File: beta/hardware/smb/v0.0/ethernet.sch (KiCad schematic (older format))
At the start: 20 parts, among them J201 HR911105_RJ45, U201 ENC28J60, X201 25MHz

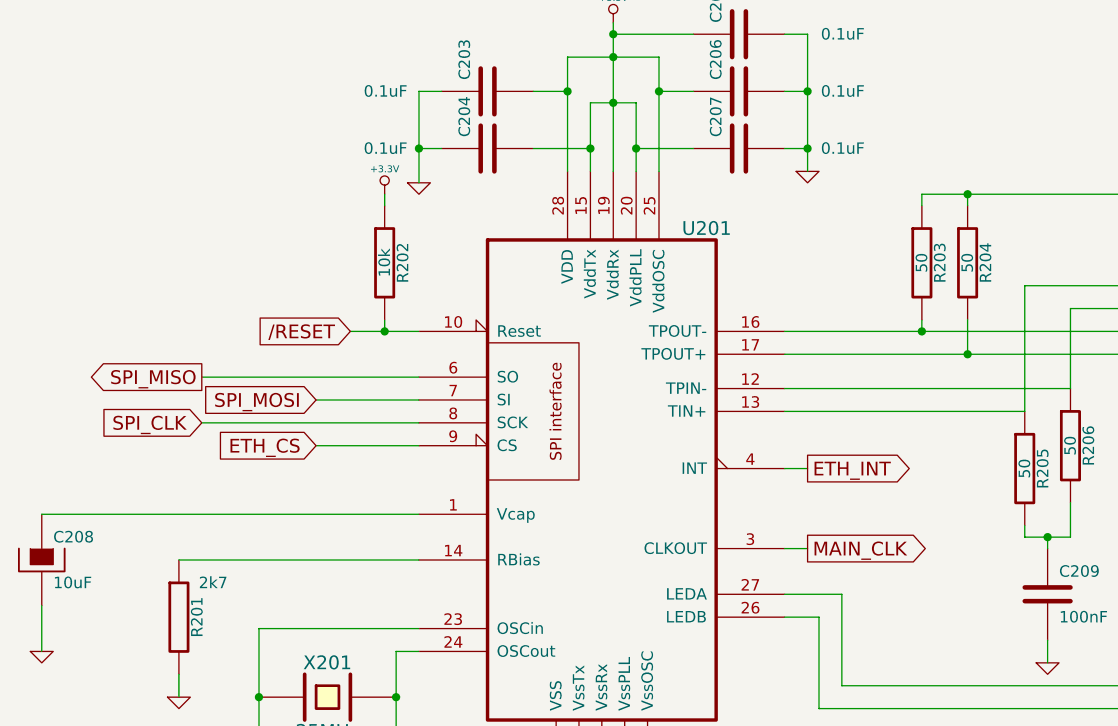
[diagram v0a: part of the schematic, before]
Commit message: SPI, clock, I2C, Misc schematic upgrade
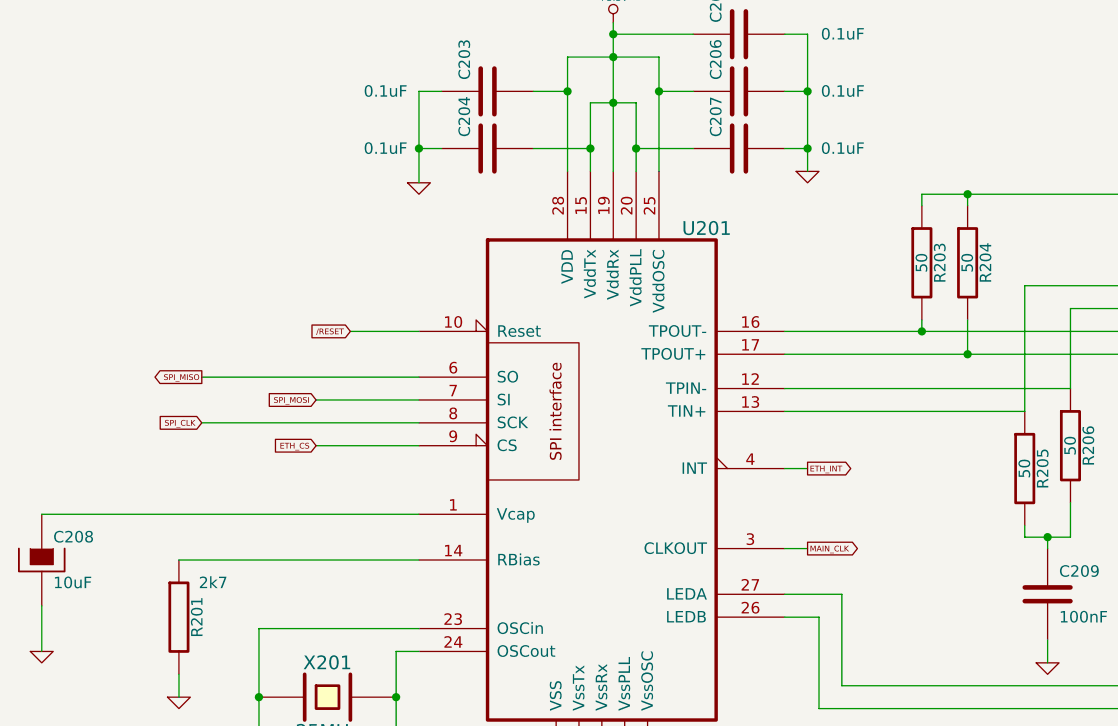
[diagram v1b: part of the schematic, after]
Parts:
- removed R202: 10k, symbol R
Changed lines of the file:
@@
-EESchema Schematic File Version 2  date 01/05/2012 18:36:30
+EESchema Schematic File Version 2  date 02/05/2012 01:38:42
 LIBS:power
 LIBS:device
@@
 LIBS:valves
 LIBS:hr911105_rj45
+LIBS:Small_connectors
 LIBS:SMB-cache
 EELAYER 25  0
@@
 	7900 3050 6650 3050
 Wire Wire Line
-	4900 2800 4900 2750
-Wire Wire Line
 	6750 3400 6650 3400
 Wire Wire Line
@@
 	6650 3750 6750 3750
 Wire Wire Line
-	4900 2200 4900 2250
-Wire Wire Line
 	4750 2800 5050 2800
-Connection ~ 4900 2800
 Wire Wire Line
 	6650 3150 7700 3150
@@
 $EndComp
 $Comp
-L +3.3V #PWR211
+L +3.3V #PWR05
 U 1 1 4FA00F89
 P 8550 1500
-F 0 "#PWR211" H 8550 1460 30  0001 C CNN
+F 0 "#PWR05" H 8550 1460 30  0001 C CNN
 F 1 "+3.3V" H 8550 1610 30  0000 C CNN
 	1    8550 1500
@@
 $EndComp
 $Comp
-L GND #PWR212
+L GND #PWR06
 U 1 1 4FA00F53
 P 8550 3700
-F 0 "#PWR212" H 8550 3700 30  0001 C CNN
+F 0 "#PWR06" H 8550 3700 30  0001 C CNN
 F 1 "GND" H 8550 3630 30  0001 C CNN
 	1    8550 3700
@@
 $EndComp
 $Comp
-L GND #PWR213
+L GND #PWR07
 U 1 1 4FA00C7B
 P 9450 3900
-F 0 "#PWR213" H 9450 3900 30  0001 C CNN
+F 0 "#PWR07" H 9450 3900 30  0001 C CNN
 F 1 "GND" H 9450 3830 30  0001 C CNN
 	1    9450 3900
@@
 $EndComp
 $Comp
-L GND #PWR214
+L GND #PWR08
 U 1 1 4FA00C63
 P 10300 4350
-F 0 "#PWR214" H 10300 4350 30  0001 C CNN
+F 0 "#PWR08" H 10300 4350 30  0001 C CNN
 F 1 "GND" H 10300 4280 30  0001 C CNN
 	1    10300 4350
@@
 $EndComp
 $Comp
-L GND #PWR210
+L GND #PWR09
 U 1 1 4F9FF676
 P 7800 4250
-F 0 "#PWR210" H 7800 4250 30  0001 C CNN
+F 0 "#PWR09" H 7800 4250 30  0001 C CNN
 F 1 "GND" H 7800 4180 30  0001 C CNN
 	1    7800 4250
@@
 	1    0    0    -1
 $EndComp
-Text GLabel 4750 2800 0    60   Input ~ 0
+Text GLabel 4750 2800 0    25   Input ~ 0
 /RESET
-$Comp
-L +3.3V #PWR204
-U 1 1 4F9FF3CF
-P 4900 2200
-F 0 "#PWR204" H 4900 2160 30  0001 C CNN
-F 1 "+3.3V" H 4900 2310 30  0000 C CNN
-	1    4900 2200
-	1    0    0    -1
-$EndComp
-$Comp
-L R R202
-U 1 1 4F9FF39B
-P 4900 2500
-F 0 "R202" V 4980 2500 50  0000 C CNN
-F 1 "10k" V 4900 2500 50  0000 C CNN
-	1    4900 2500
-	1    0    0    -1
-$EndComp
-Text GLabel 6750 3400 2    60   Output ~ 0
+Text GLabel 6750 3400 2    25   Output ~ 0
 ETH_INT
-Text GLabel 6750 3750 2    60   Output ~ 0
+Text GLabel 6750 3750 2    25   Output ~ 0
 MAIN_CLK
-Text GLabel 4100 3000 0    60   Output ~ 0
+Text GLabel 4100 3000 0    25   Output ~ 0
 SPI_MISO
-Text GLabel 4600 3100 0    60   Input ~ 0
+Text GLabel 4600 3100 0    25   Input ~ 0
 SPI_MOSI
-Text GLabel 4600 3300 0    60   Input ~ 0
+Text GLabel 4600 3300 0    25   Input ~ 0
 ETH_CS
-Text GLabel 4100 3200 0    60   Input ~ 0
+Text GLabel 4100 3200 0    25   Input ~ 0
 SPI_CLK
 $Comp
-L GND #PWR201
+L GND #PWR011
 U 1 1 4F9FEE21
 P 3400 4200
-F 0 "#PWR201" H 3400 4200 30  0001 C CNN
+F 0 "#PWR011" H 3400 4200 30  0001 C CNN
 F 1 "GND" H 3400 4130 30  0001 C CNN
 	1    3400 4200
@@
 $EndComp
 $Comp
-L GND #PWR202
+L GND #PWR012
 U 1 1 4F9FEE1E
 P 4000 4400
-F 0 "#PWR202" H 4000 4400 30  0001 C CNN
+F 0 "#PWR012" H 4000 4400 30  0001 C CNN
 F 1 "GND" H 4000 4330 30  0001 C CNN
 	1    4000 4400
@@
 $EndComp
 $Comp
-L GND #PWR206
+L GND #PWR013
 U 1 1 4F9FC462
 P 5050 2150
-F 0 "#PWR206" H 5050 2150 30  0001 C CNN
+F 0 "#PWR013" H 5050 2150 30  0001 C CNN
 F 1 "GND" H 5050 2080 30  0001 C CNN
 	1    5050 2150
@@
 $EndComp
 $Comp
-L GND #PWR209
+L GND #PWR014
 U 1 1 4F9FC45C
 P 6750 2100
-F 0 "#PWR209" H 6750 2100 30  0001 C CNN
+F 0 "#PWR014" H 6750 2100 30  0001 C CNN
 F 1 "GND" H 6750 2030 30  0001 C CNN
 	1    6750 2100
@@
 $EndComp
 $Comp
-L +3.3V #PWR208
+L +3.3V #PWR015
 U 1 1 4F9FC2EE
 P 5900 1450
-F 0 "#PWR208" H 5900 1410 30  0001 C CNN
+F 0 "#PWR015" H 5900 1410 30  0001 C CNN
 F 1 "+3.3V" H 5900 1560 30  0000 C CNN
 	1    5900 1450
@@
 $EndComp
 $Comp
-L GND #PWR203
+L GND #PWR016
 U 1 1 4F9D7261
 P 4350 5050
-F 0 "#PWR203" H 4350 5050 30  0001 C CNN
+F 0 "#PWR016" H 4350 5050 30  0001 C CNN
 F 1 "GND" H 4350 4980 30  0001 C CNN
 	1    4350 5050
@@
 $EndComp
 $Comp
-L GND #PWR205
+L GND #PWR017
 U 1 1 4F9D725B
 P 4950 5050
-F 0 "#PWR205" H 4950 5050 30  0001 C CNN
+F 0 "#PWR017" H 4950 5050 30  0001 C CNN
 F 1 "GND" H 4950 4980 30  0001 C CNN
 	1    4950 5050
@@
 $EndComp
 $Comp
-L GND #PWR207
+L GND #PWR018
 U 1 1 4F9D6E29
 P 5850 4950
-F 0 "#PWR207" H 5850 4950 30  0001 C CNN
+F 0 "#PWR018" H 5850 4950 30  0001 C CNN
 F 1 "GND" H 5850 4880 30  0001 C CNN
 	1    5850 4950

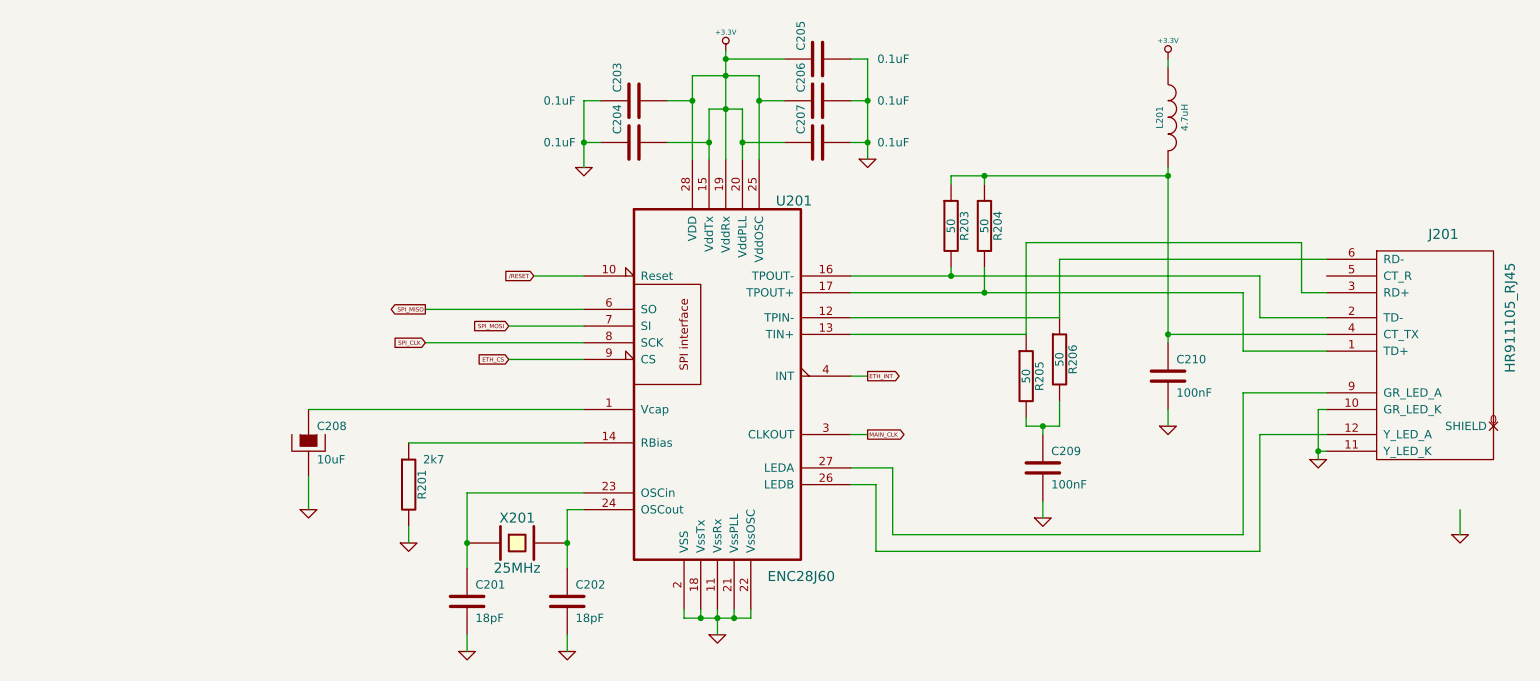
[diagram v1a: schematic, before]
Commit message: Some work on the SMD version of the SMB
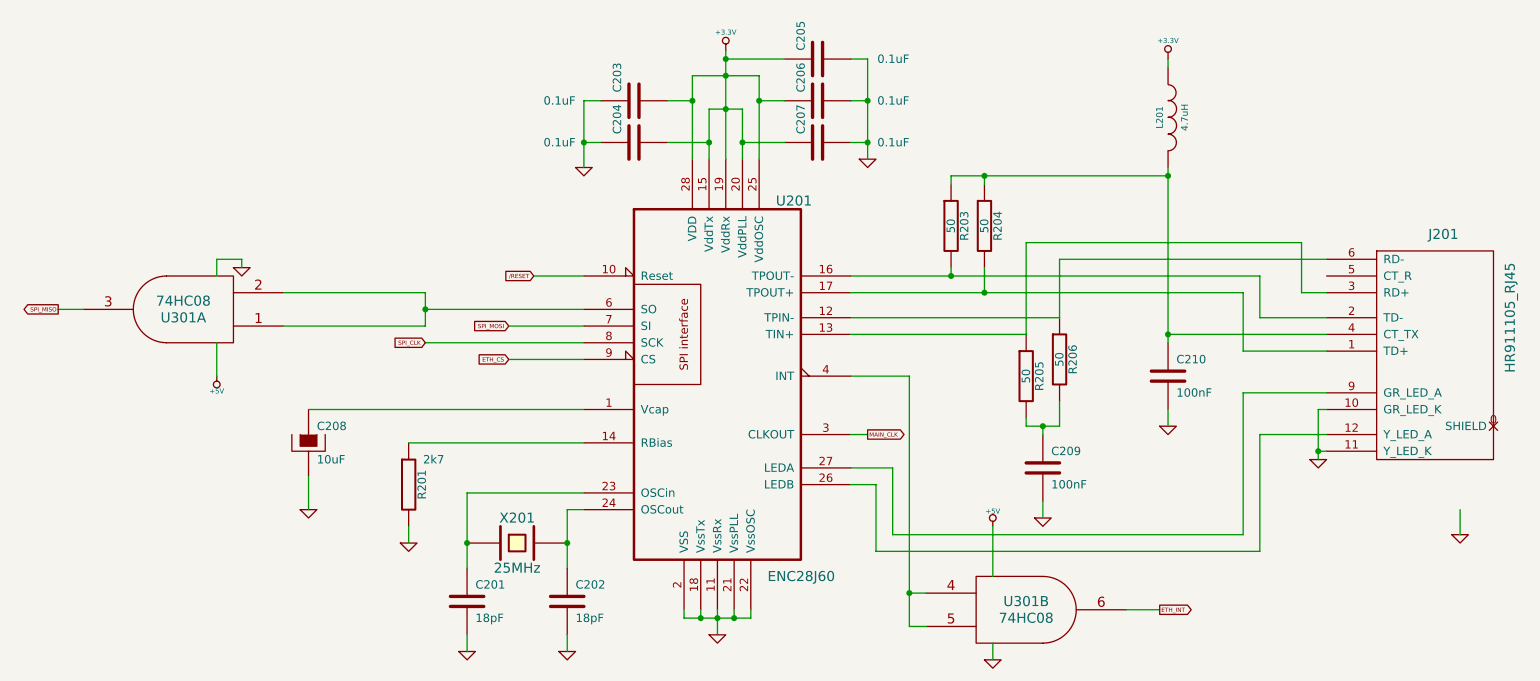
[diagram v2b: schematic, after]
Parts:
- added U301: 74HC08, symbol 74HC08
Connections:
- net ETH_INT: now also U301.6; no longer U201.4 (INT)
- net GND: now also U301.7 (GND), U301.7 (GND)
- net SPI_MISO: now also U301.3; no longer U201.6 (SO)
- new net: U201.4 (INT), U301.4, U301.5
- new net: U201.6 (SO), U301.1, U301.2
- new net +5V: U301.14 (VCC), U301.14 (VCC)
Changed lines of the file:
@@
-EESchema Schematic File Version 2  date 02/05/2012 01:38:42
+EESchema Schematic File Version 2  date 17/06/2012 23:05:58
 LIBS:power
 LIBS:device
@@
 LIBS:hr911105_rj45
 LIBS:Small_connectors
+LIBS:74hc08
+LIBS:lm1117imp-3
 LIBS:SMB-cache
 EELAYER 25  0
@@
 $Descr A4 11700 8267
 encoding utf-8
-Sheet 2 2
+Sheet 3 3
 Title ""
-Date "1 may 2012"
+Date "17 jun 2012"
 Rev ""
 Comp ""
@@
 Comment4 ""
 $EndDescr
+Wire Wire Line
+	7500 4300 7500 4600
+Wire Wire Line
+	3000 2750 3000 2700
+Wire Wire Line
+	3000 2700 2850 2700
+Wire Wire Line
+	2850 2700 2850 2800
+Wire Wire Line
+	8300 4800 8500 4800
+Wire Wire Line
+	7100 4900 7000 4900
+Wire Wire Line
+	7000 4900 7000 3400
+Wire Wire Line
+	7000 3400 6650 3400
+Connection ~ 4100 3000
+Wire Wire Line
+	3250 3100 4100 3100
+Wire Wire Line
+	4100 3100 4100 2900
 Connection ~ 8550 2200
 Wire Wire Line
@@
 	7900 3050 6650 3050
 Wire Wire Line
-	6750 3400 6650 3400
-Wire Wire Line
 	4600 3300 5050 3300
 Wire Wire Line
@@
 	7250 2200 7250 2250
 Connection ~ 7450 2200
+Wire Wire Line
+	4100 2900 3250 2900
+Wire Wire Line
+	2050 3000 1900 3000
+Wire Wire Line
+	7100 4700 7000 4700
+Connection ~ 7000 4700
+Wire Wire Line
+	2850 3200 2850 3400
+Wire Wire Line
+	7500 5000 7500 5100
+$Comp
+L +5V #PWR311
+U 1 1 4FDE1BE4
+P 7500 4300
+F 0 "#PWR311" H 7500 4390 20  0001 C CNN
+F 1 "+5V" H 7500 4390 30  0000 C CNN
+	1    7500 4300
+	1    0    0    -1
+$EndComp
+$Comp
+L GND #PWR312
+U 1 1 4FDE1B8D
+P 7500 5100
+F 0 "#PWR312" H 7500 5100 30  0001 C CNN
+F 1 "GND" H 7500 5030 30  0001 C CNN
+	1    7500 5100
+	1    0    0    -1
+$EndComp
+$Comp
+L GND #PWR302
+U 1 1 4FDE1B70
+P 3000 2750
+F 0 "#PWR302" H 3000 2750 30  0001 C CNN
+F 1 "GND" H 3000 2680 30  0001 C CNN
+	1    3000 2750
+	1    0    0    -1
+$EndComp
+$Comp
+L +5V #PWR301
+U 1 1 4FDE1B61
+P 2850 3400
+F 0 "#PWR301" H 2850 3490 20  0001 C CNN
+F 1 "+5V" H 2850 3490 30  0000 C CNN
+	1    2850 3400
+	-1   0    0    1
+$EndComp
+$Comp
+L 74HC08 U301
+U 2 1 4FDE1879
+P 7700 4800
+F 0 "U301" H 7700 4850 60  0000 C CNN
+F 1 "74HC08" H 7700 4750 60  0000 C CNN
+	2    7700 4800
+	1    0    0    -1
+$EndComp
+$Comp
+L 74HC08 U301
+U 1 1 4FDE1808
+P 2650 3000
+F 0 "U301" H 2650 3050 60  0000 C CNN
+F 1 "74HC08" H 2650 2950 60  0000 C CNN
+	1    2650 3000
+	-1   0    0    1
+$EndComp
 $Comp
 L R R204
@@
 $EndComp
 $Comp
-L +3.3V #PWR05
+L +3.3V #PWR314
 U 1 1 4FA00F89
 P 8550 1500
-F 0 "#PWR05" H 8550 1460 30  0001 C CNN
+F 0 "#PWR314" H 8550 1460 30  0001 C CNN
 F 1 "+3.3V" H 8550 1610 30  0000 C CNN
 	1    8550 1500
@@
 $EndComp
 $Comp
-L GND #PWR06
+L GND #PWR315
 U 1 1 4FA00F53
 P 8550 3700
-F 0 "#PWR06" H 8550 3700 30  0001 C CNN
+F 0 "#PWR315" H 8550 3700 30  0001 C CNN
 F 1 "GND" H 8550 3630 30  0001 C CNN
 	1    8550 3700
@@
 $EndComp
 $Comp
-L GND #PWR07
+L GND #PWR316
 U 1 1 4FA00C7B
 P 9450 3900
-F 0 "#PWR07" H 9450 3900 30  0001 C CNN
+F 0 "#PWR316" H 9450 3900 30  0001 C CNN
 F 1 "GND" H 9450 3830 30  0001 C CNN
 	1    9450 3900
@@
 $EndComp
 $Comp
-L GND #PWR08
+L GND #PWR317
 U 1 1 4FA00C63
 P 10300 4350
-F 0 "#PWR08" H 10300 4350 30  0001 C CNN
+F 0 "#PWR317" H 10300 4350 30  0001 C CNN
 F 1 "GND" H 10300 4280 30  0001 C CNN
 	1    10300 4350
@@
 $EndComp
 $Comp
-L GND #PWR09
+L GND #PWR313
 U 1 1 4F9FF676
 P 7800 4250
-F 0 "#PWR09" H 7800 4250 30  0001 C CNN
+F 0 "#PWR313" H 7800 4250 30  0001 C CNN
 F 1 "GND" H 7800 4180 30  0001 C CNN
 	1    7800 4250
@@
 Text GLabel 4750 2800 0    25   Input ~ 0
 /RESET
-Text GLabel 6750 3400 2    25   Output ~ 0
+Text GLabel 8500 4800 2    25   Output ~ 0
 ETH_INT
 Text GLabel 6750 3750 2    25   Output ~ 0
 MAIN_CLK
-Text GLabel 4100 3000 0    25   Output ~ 0
+Text GLabel 1900 3000 0    25   Output ~ 0
 SPI_MISO
 Text GLabel 4600 3100 0    25   Input ~ 0
@@
 SPI_CLK
 $Comp
-L GND #PWR011
+L GND #PWR303
 U 1 1 4F9FEE21
 P 3400 4200
-F 0 "#PWR011" H 3400 4200 30  0001 C CNN
+F 0 "#PWR303" H 3400 4200 30  0001 C CNN
 F 1 "GND" H 3400 4130 30  0001 C CNN
 	1    3400 4200
@@
 $EndComp
 $Comp
-L GND #PWR012
+L GND #PWR304
 U 1 1 4F9FEE1E
 P 4000 4400
-F 0 "#PWR012" H 4000 4400 30  0001 C CNN
+F 0 "#PWR304" H 4000 4400 30  0001 C CNN
 F 1 "GND" H 4000 4330 30  0001 C CNN
 	1    4000 4400
@@
 $EndComp
 $Comp
-L GND #PWR013
+L GND #PWR307
 U 1 1 4F9FC462
 P 5050 2150
-F 0 "#PWR013" H 5050 2150 30  0001 C CNN
+F 0 "#PWR307" H 5050 2150 30  0001 C CNN
 F 1 "GND" H 5050 2080 30  0001 C CNN
 	1    5050 2150
@@
 $EndComp
 $Comp
-L GND #PWR014
+L GND #PWR310
 U 1 1 4F9FC45C
 P 6750 2100
-F 0 "#PWR014" H 6750 2100 30  0001 C CNN
+F 0 "#PWR310" H 6750 2100 30  0001 C CNN
 F 1 "GND" H 6750 2030 30  0001 C CNN
 	1    6750 2100
@@
 $EndComp
 $Comp
-L +3.3V #PWR015
+L +3.3V #PWR309
 U 1 1 4F9FC2EE
 P 5900 1450
-F 0 "#PWR015" H 5900 1410 30  0001 C CNN
+F 0 "#PWR309" H 5900 1410 30  0001 C CNN
 F 1 "+3.3V" H 5900 1560 30  0000 C CNN
 	1    5900 1450
@@
 $EndComp
 $Comp
-L GND #PWR016
+L GND #PWR305
 U 1 1 4F9D7261
 P 4350 5050
-F 0 "#PWR016" H 4350 5050 30  0001 C CNN
+F 0 "#PWR305" H 4350 5050 30  0001 C CNN
 F 1 "GND" H 4350 4980 30  0001 C CNN
 	1    4350 5050
@@
 $EndComp
 $Comp
-L GND #PWR017
+L GND #PWR306
 U 1 1 4F9D725B
 P 4950 5050
-F 0 "#PWR017" H 4950 5050 30  0001 C CNN
+F 0 "#PWR306" H 4950 5050 30  0001 C CNN
 F 1 "GND" H 4950 4980 30  0001 C CNN
 	1    4950 5050
@@
 $EndComp
 $Comp
-L GND #PWR018
+L GND #PWR308
 U 1 1 4F9D6E29
 P 5850 4950
-F 0 "#PWR018" H 5850 4950 30  0001 C CNN
+F 0 "#PWR308" H 5850 4950 30  0001 C CNN
 F 1 "GND" H 5850 4880 30  0001 C CNN
 	1    5850 4950
